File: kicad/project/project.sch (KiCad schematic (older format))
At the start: 38 parts, among them J1 SWD, Q1 MMBT3906, Q2 MMBT3906, Q3 IRF3205, Q4 MMBT3904, U1 NCV4264-2CST33T3G, U2 STM32L031F4Px

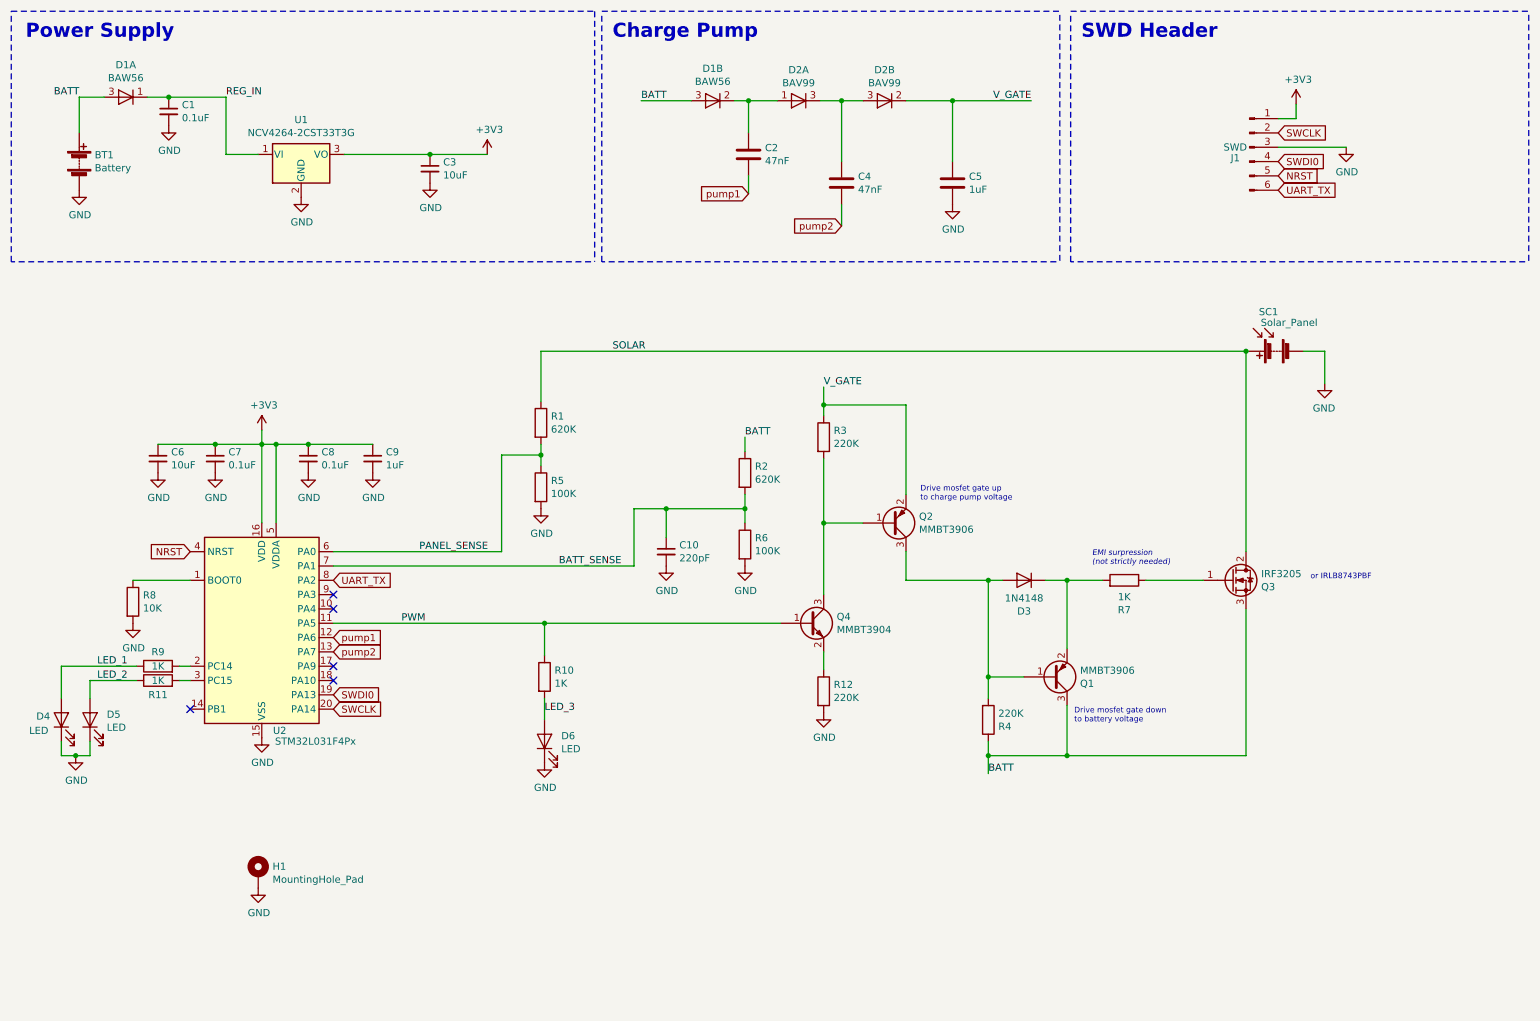
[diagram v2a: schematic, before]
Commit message: Clearer schematic
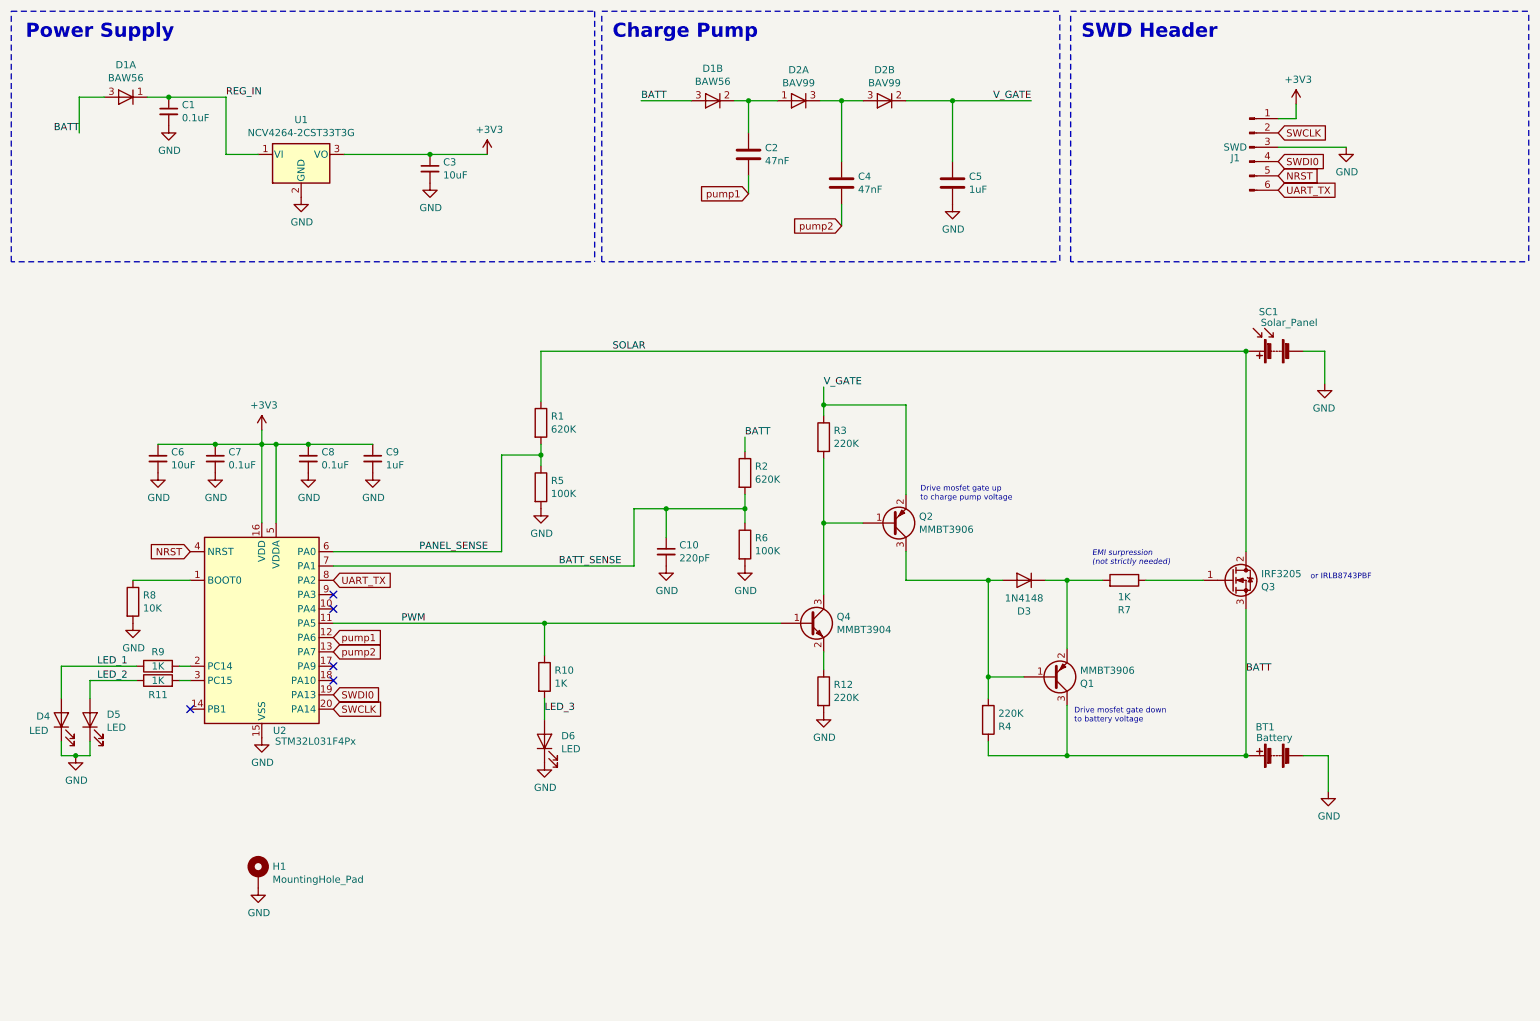
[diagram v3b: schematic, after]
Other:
- moved on the sheet: BT1
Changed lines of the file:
@@
 L power:GND #PWR06
 U 1 1 5C80809F
-P 1025 1850
-F 0 "#PWR06" H 1025 1600 50  0001 C CNN
-F 1 "GND" H 1030 1677 50  0000 C CNN
-F 2 "" H 1025 1850 50  0001 C CNN
-F 3 "" H 1025 1850 50  0001 C CNN
-	1    1025 1850
+P 9750 6050
+F 0 "#PWR06" H 9750 5800 50  0001 C CNN
+F 1 "GND" H 9755 5877 50  0000 C CNN
+F 2 "" H 9750 6050 50  0001 C CNN
+F 3 "" H 9750 6050 50  0001 C CNN
+	1    9750 6050
 	1    0    0    -1
 $EndComp
@@
 L Device:Battery BT1
 U 1 1 5CDC3C72
-P 1025 1650
-F 0 "BT1" H 1133 1696 50  0000 L CNN
-F 1 "Battery" H 1133 1605 50  0000 L CNN
-F 2 "TerminalBlock:TerminalBlock_bornier-2_P5.08mm" V 1025 1710 50  0001 C CNN
-F 3 "~" V 1025 1710 50  0001 C CNN
-	1    1025 1650
-	1    0    0    -1
+P 9375 5800
+F 0 "BT1" V 9575 5800 50  0000 L CNN
+F 1 "Battery" V 9500 5675 50  0000 L CNN
+F 2 "TerminalBlock:TerminalBlock_bornier-2_P5.08mm" V 9375 5860 50  0001 C CNN
+F 3 "~" V 9375 5860 50  0001 C CNN
+	1    9375 5800
+	0    -1   -1   0
 $EndComp
 $Comp
@@
 	1500 1200 1650 1200
 Connection ~ 1650 1200
-Text Label 1025 1200 2    50   ~ 0
+Text Label 1025 1450 2    50   ~ 0
 BATT
 $Comp
@@
 Wire Wire Line
 	6800 4575 6800 4375
-Text Label 7375 5925 0    50   ~ 0
+Text Label 9175 5225 0    50   ~ 0
 BATT
-Wire Wire Line
-	7375 5925 7375 5800
 Wire Wire Line
 	7375 5400 7375 5250
@@
 Wire Wire Line
 	7925 5800 7375 5800
-Connection ~ 7375 5800
 Wire Wire Line
 	7375 5800 7375 5700
@@
 Wire Wire Line
 	9175 2975 9175 4375
+Connection ~ 9175 5800
+Wire Wire Line
+	9575 5800 9750 5800
+Wire Wire Line
+	9750 5800 9750 6050
 $EndSCHEMATC

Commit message: Allow for solid connection to mosfet
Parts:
- BT1: footprint TerminalBlock:TerminalBlock_bornier-2_P5.08mm -> theapi:TerminalBlock_bornier-2_P5.08mm
- SC1: footprint TerminalBlock:TerminalBlock_bornier-2_P5.08mm -> theapi:TerminalBlock_flipped_bornier-2_P5.08mm
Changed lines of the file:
@@
 F 0 "SC1" V 9100 2950 50  0000 L CNN
 F 1 "Solar_Panel" V 9175 2675 50  0000 L CNN
-F 2 "TerminalBlock:TerminalBlock_bornier-2_P5.08mm" V 9375 3035 50  0001 C CNN
+F 2 "theapi:TerminalBlock_flipped_bornier-2_P5.08mm" V 9375 3035 50  0001 C CNN
 F 3 "~" V 9375 3035 50  0001 C CNN
 	1    9375 2975
@@
 F 0 "BT1" V 9575 5800 50  0000 L CNN
 F 1 "Battery" V 9500 5675 50  0000 L CNN
-F 2 "TerminalBlock:TerminalBlock_bornier-2_P5.08mm" V 9375 5860 50  0001 C CNN
+F 2 "theapi:TerminalBlock_bornier-2_P5.08mm" V 9375 5860 50  0001 C CNN
 F 3 "~" V 9375 5860 50  0001 C CNN
 	1    9375 5800

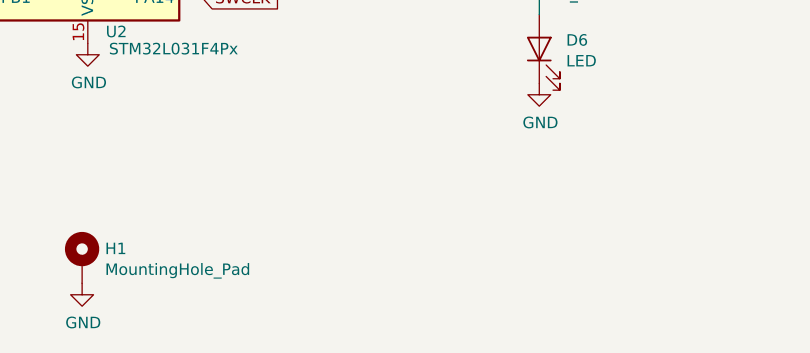
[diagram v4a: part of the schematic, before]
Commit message: Heart to go in the potting mould
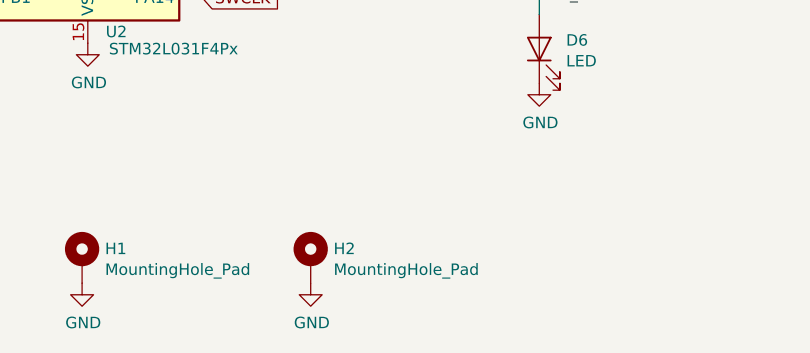
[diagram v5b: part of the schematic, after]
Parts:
- added H2: MountingHole_Pad, MountingHole:MountingHole_3.2mm_M3_Pad, symbol Mechanical:MountingHole_Pad
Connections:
- net GND: now also H2.1
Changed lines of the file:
@@
 Text Label 4275 5500 0    50   ~ 0
 LED_3
-$Comp
-L Mechanical:MountingHole_Pad H1
-U 1 1 5C8B15A7
-P 2275 6625
-F 0 "H1" H 2375 6676 50  0000 L CNN
-F 1 "MountingHole_Pad" H 2375 6585 50  0000 L CNN
-F 2 "MountingHole:MountingHole_3.2mm_M3_Pad" H 2275 6625 50  0001 C CNN
-F 3 "~" H 2275 6625 50  0001 C CNN
-	1    2275 6625
-	1    0    0    -1
-$EndComp
-$Comp
-L power:GND #PWR023
-U 1 1 5C8BA2A9
-P 2275 6725
-F 0 "#PWR023" H 2275 6475 50  0001 C CNN
-F 1 "GND" H 2280 6552 50  0000 C CNN
-F 2 "" H 2275 6725 50  0001 C CNN
-F 3 "" H 2275 6725 50  0001 C CNN
-	1    2275 6725
-	1    0    0    -1
-$EndComp
 Wire Wire Line
 	2800 4475 4900 4475
@@
 Wire Wire Line
 	9750 5800 9750 6050
+$Comp
+L power:GND #PWR023
+U 1 1 5C8BA2A9
+P 2275 6725
+F 0 "#PWR023" H 2275 6475 50  0001 C CNN
+F 1 "GND" H 2280 6552 50  0000 C CNN
+F 2 "" H 2275 6725 50  0001 C CNN
+F 3 "" H 2275 6725 50  0001 C CNN
+	1    2275 6725
+	1    0    0    -1
+$EndComp
+$Comp
+L Mechanical:MountingHole_Pad H1
+U 1 1 5C8B15A7
+P 2275 6625
+F 0 "H1" H 2375 6676 50  0000 L CNN
+F 1 "MountingHole_Pad" H 2375 6585 50  0000 L CNN
+F 2 "MountingHole:MountingHole_3.2mm_M3_Pad" H 2275 6625 50  0001 C CNN
+F 3 "~" H 2275 6625 50  0001 C CNN
+	1    2275 6625
+	1    0    0    -1
+$EndComp
+$Comp
+L power:GND #PWR024
+U 1 1 5CE1EE4D
+P 3275 6725
+F 0 "#PWR024" H 3275 6475 50  0001 C CNN
+F 1 "GND" H 3280 6552 50  0000 C CNN
+F 2 "" H 3275 6725 50  0001 C CNN
+F 3 "" H 3275 6725 50  0001 C CNN
+	1    3275 6725
+	1    0    0    -1
+$EndComp
+$Comp
+L Mechanical:MountingHole_Pad H2
+U 1 1 5CE1EE53
+P 3275 6625
+F 0 "H2" H 3375 6676 50  0000 L CNN
+F 1 "MountingHole_Pad" H 3375 6585 50  0000 L CNN
+F 2 "MountingHole:MountingHole_3.2mm_M3_Pad" H 3275 6625 50  0001 C CNN
+F 3 "~" H 3275 6625 50  0001 C CNN
+	1    3275 6625
+	1    0    0    -1
+$EndComp
 $EndSCHEMATC

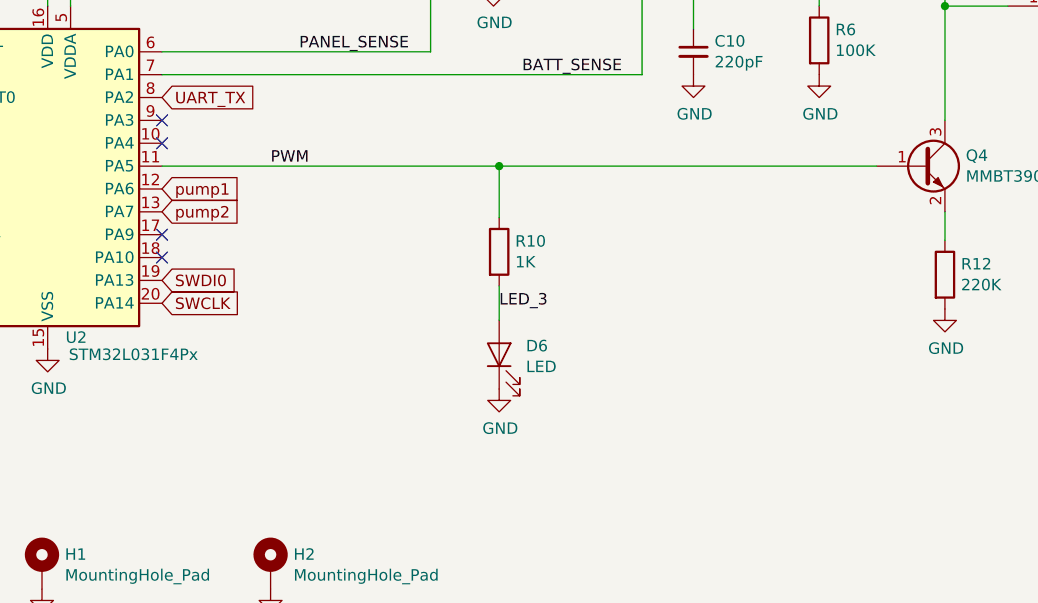
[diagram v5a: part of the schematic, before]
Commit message: Layout change
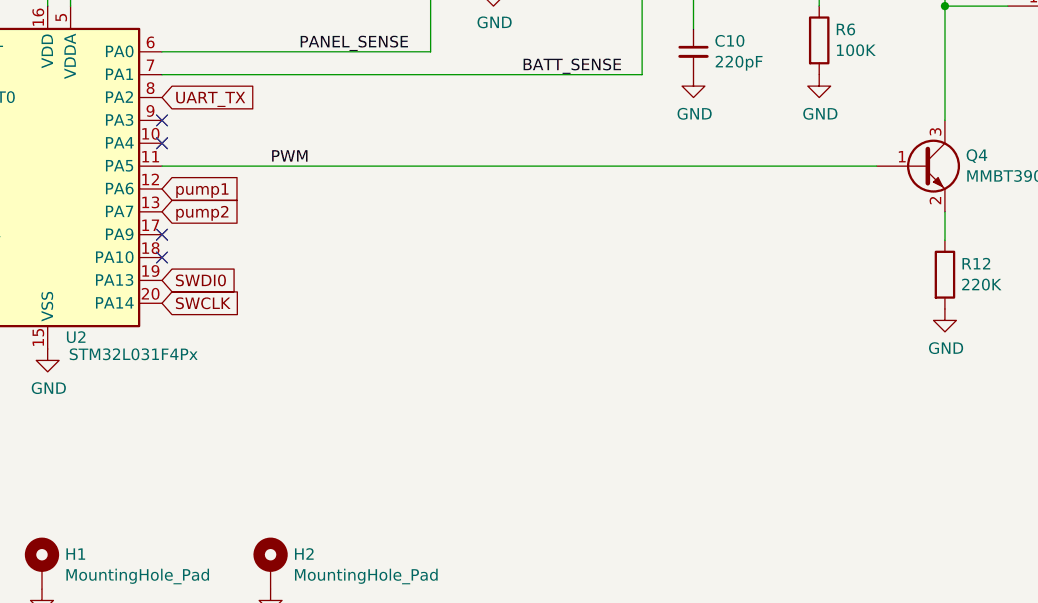
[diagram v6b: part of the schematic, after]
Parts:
- removed D6: LED, LED_SMD:LED_0805_2012Metric_Pad1.15x1.40mm_HandSolder, symbol Device:LED
- removed R10: 1K, Resistor_SMD:R_0603_1608Metric_Pad1.05x0.95mm_HandSolder, symbol Device:R
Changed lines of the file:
@@
 $EndComp
-$Comp
-L Device:R R10
-U 1 1 5C7C0432
-P 4275 5250
-F 0 "R10" H 4345 5296 50  0000 L CNN
-F 1 "1K" H 4345 5205 50  0000 L CNN
-F 2 "Resistor_SMD:R_0603_1608Metric_Pad1.05x0.95mm_HandSolder" V 4205 5250 50  0001 C CNN
-F 3 "~" H 4275 5250 50  0001 C CNN
-	1    4275 5250
-	1    0    0    -1
-$EndComp
-$Comp
-L Device:LED D6
-U 1 1 5C7C051B
-P 4275 5700
-F 0 "D6" V 4313 5583 50  0000 R CNN
-F 1 "LED" V 4222 5583 50  0000 R CNN
-F 2 "LED_SMD:LED_0805_2012Metric_Pad1.15x1.40mm_HandSolder" H 4275 5700 50  0001 C CNN
-F 3 "~" H 4275 5700 50  0001 C CNN
-	1    4275 5700
-	0    -1   -1   0
-$EndComp
-$Comp
-L power:GND #PWR022
-U 1 1 5C7C05D8
-P 4275 5850
-F 0 "#PWR022" H 4275 5600 50  0001 C CNN
-F 1 "GND" H 4280 5677 50  0000 C CNN
-F 2 "" H 4275 5850 50  0001 C CNN
-F 3 "" H 4275 5850 50  0001 C CNN
-	1    4275 5850
-	1    0    0    -1
-$EndComp
-Wire Wire Line
-	4275 5550 4275 5400
 $Comp
 L Device:LED D4
@@
 	1100 5800 1000 5800
 Connection ~ 1000 5800
-Wire Wire Line
-	4275 5100 4275 4875
 NoConn ~ 2800 4675
 Text Label 1150 5275 0    50   ~ 0
 LED_2
-Text Label 4275 5500 0    50   ~ 0
-LED_3
 Wire Wire Line
 	2800 4475 4900 4475
@@
 	1    0    0    -1
 $EndComp
-Wire Wire Line
-	2800 4875 4275 4875
 $Comp
 L power:GND #PWR018
@@
 	-1   0    0    -1
 $EndComp
-Connection ~ 4275 4875
-Wire Wire Line
-	4275 4875 5925 4875
 Text Label 2050 1200 0    50   ~ 0
 REG_IN
@@
 	1    0    0    -1
 $EndComp
+Wire Wire Line
+	2800 4875 5925 4875
 $EndSCHEMATC

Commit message: Test points
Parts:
- added TP1, TP2, TP3, TP4, TP5: TestPoint, Connectors_TestPoints:Test_Point_Pad_d1.0mm, symbol Connector:TestPoint
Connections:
- net BATT_SENSE: now also TP4.1
- net PWM: now also TP5.1
- net V_GATE: now also TP1.1
- net pump1: now also TP2.1
- net pump2: now also TP3.1
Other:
- moved on the sheet: C4
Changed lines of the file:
@@
 LED_2
 Wire Wire Line
-	2800 4475 4900 4475
+	2800 4475 4300 4475
 $Comp
 L Device:Battery BT1
@@
 Text GLabel 6350 2100 0    50   Input ~ 0
 pump2
-Text GLabel 5700 1875 0    50   Input ~ 0
+Text GLabel 5700 2100 0    50   Input ~ 0
 pump1
 Text Notes 4750 800  0    98   ~ 20
@@
 L Device:C C4
 U 1 1 5CDB9EB6
-P 6350 1800
-F 0 "C4" H 6465 1846 50  0000 L CNN
-F 1 "47nF" H 6465 1755 50  0000 L CNN
-F 2 "Capacitor_SMD:C_0603_1608Metric_Pad1.05x0.95mm_HandSolder" H 6388 1650 50  0001 C CNN
-F 3 "~" H 6350 1800 50  0001 C CNN
-	1    6350 1800
+P 6350 1600
+F 0 "C4" H 6465 1646 50  0000 L CNN
+F 1 "47nF" H 6465 1555 50  0000 L CNN
+F 2 "Capacitor_SMD:C_0603_1608Metric_Pad1.05x0.95mm_HandSolder" H 6388 1450 50  0001 C CNN
+F 3 "~" H 6350 1600 50  0001 C CNN
+	1    6350 1600
 	1    0    0    -1
 $EndComp
@@
 	5700 1225 5900 1225
 Wire Wire Line
-	6350 1650 6350 1225
+	6350 1450 6350 1225
 Connection ~ 6350 1225
 Wire Wire Line
 	6350 1225 6500 1225
 Wire Wire Line
-	6350 1950 6350 2100
-Wire Wire Line
-	5700 1750 5700 1875
+	6350 1750 6350 1900
+Wire Wire Line
+	5700 1750 5700 1900
 Text Label 4950 1225 0    50   ~ 0
 BATT
@@
 Connection ~ 7125 1225
 Wire Wire Line
-	7125 1225 7675 1225
+	7125 1225 7225 1225
 Text Label 5675 3575 0    50   ~ 0
 BATT
@@
 $EndComp
 Wire Wire Line
-	2800 4875 5925 4875
+	2800 4875 4300 4875
+$Comp
+L Connector:TestPoint TP5
+U 1 1 5CE45D7F
+P 4300 4875
+F 0 "TP5" H 4350 5175 50  0000 R CNN
+F 1 "TestPoint" H 4450 5100 50  0000 R CNN
+F 2 "Connectors_TestPoints:Test_Point_Pad_d1.0mm" H 4500 4875 50  0001 C CNN
+F 3 "~" H 4500 4875 50  0001 C CNN
+	1    4300 4875
+	-1   0    0    1
+$EndComp
+Connection ~ 4300 4875
+Wire Wire Line
+	4300 4875 5925 4875
+$Comp
+L Connector:TestPoint TP2
+U 1 1 5CE460AF
+P 5700 1900
+F 0 "TP2" V 5725 2225 50  0000 C CNN
+F 1 "TestPoint" V 5800 2125 50  0000 C CNN
+F 2 "Connectors_TestPoints:Test_Point_Pad_d1.0mm" H 5900 1900 50  0001 C CNN
+F 3 "~" H 5900 1900 50  0001 C CNN
+	1    5700 1900
+	0    -1   -1   0
+$EndComp
+Connection ~ 5700 1900
+Wire Wire Line
+	5700 1900 5700 2100
+$Comp
+L Connector:TestPoint TP3
+U 1 1 5CE49D80
+P 6350 1900
+F 0 "TP3" V 6375 2225 50  0000 C CNN
+F 1 "TestPoint" V 6450 2125 50  0000 C CNN
+F 2 "Connectors_TestPoints:Test_Point_Pad_d1.0mm" H 6550 1900 50  0001 C CNN
+F 3 "~" H 6550 1900 50  0001 C CNN
+	1    6350 1900
+	0    -1   -1   0
+$EndComp
+Connection ~ 6350 1900
+Wire Wire Line
+	6350 1900 6350 2100
+$Comp
+L Connector:TestPoint TP1
+U 1 1 5CE49E54
+P 7225 1225
+F 0 "TP1" H 7175 1525 50  0000 L CNN
+F 1 "TestPoint" H 7075 1450 50  0000 L CNN
+F 2 "Connectors_TestPoints:Test_Point_Pad_d1.0mm" H 7425 1225 50  0001 C CNN
+F 3 "~" H 7425 1225 50  0001 C CNN
+	1    7225 1225
+	1    0    0    -1
+$EndComp
+Connection ~ 7225 1225
+Wire Wire Line
+	7225 1225 7675 1225
+$Comp
+L Connector:TestPoint TP4
+U 1 1 5CE4A80C
+P 4300 4475
+F 0 "TP4" H 4350 4775 50  0000 R CNN
+F 1 "TestPoint" H 4450 4700 50  0000 R CNN
+F 2 "Connectors_TestPoints:Test_Point_Pad_d1.0mm" H 4500 4475 50  0001 C CNN
+F 3 "~" H 4500 4475 50  0001 C CNN
+	1    4300 4475
+	-1   0    0    1
+$EndComp
+Connection ~ 4300 4475
+Wire Wire Line
+	4300 4475 4900 4475
 $EndSCHEMATC

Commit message: SOD 123F
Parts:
- D3: footprint Diode_SMD:D_SOD-123 -> Diode_SMD:D_SOD-123F
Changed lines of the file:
@@
 F 0 "D3" H 7625 4359 50  0000 C CNN
 F 1 "1N4148" H 7625 4450 50  0000 C CNN
-F 2 "Diode_SMD:D_SOD-123" H 7625 4400 50  0001 C CNN
+F 2 "Diode_SMD:D_SOD-123F" H 7625 4400 50  0001 C CNN
 F 3 "http://www.nxp.com/documents/data_sheet/1N4148_1N4448.pdf" H 7625 4575 50  0001 C CNN
 	1    7625 4575
